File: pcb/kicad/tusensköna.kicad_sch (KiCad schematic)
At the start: 36 parts, among them J1 AudioJack3, J2 AudioJack3, J3 Micro_SD_Card, SW1 SW_Push, SW2 SW_Push, U1 Electrosmith_Daisy_Seed_Rev4

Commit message: issues fixed
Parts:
- removed 3V3A1, 3V3D1, A0, A6, GND1, MI1, MO1, SCK1, SCL1, SDA1, SS1, VIN1: Conn_01x01, Connector_Wire:SolderWire-0.5sqmm_1x01_D0.9mm_OD2.1mm, symbol Connector_Generic:Conn_01x01
- added J4: Conn_01x12_Pin, Connector_PinHeader_2.54mm:PinHeader_1x12_P2.54mm_Vertical, symbol Connector:Conn_01x12_Pin
- added JP1, JP2: Jumper_2_Bridged, Connector_PinHeader_2.54mm:PinHeader_1x02_P2.54mm_Vertical, symbol Jumper:Jumper_2_Bridged
- added R10, R9: 4.7k, Resistor_SMD:R_0805_2012Metric, symbol Device:R
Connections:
- net 3V3A: now also J4.12 (Pin_12)
- net 3V3D: now also J4.9 (Pin_9)
- net ADC0: now also J4.11 (Pin_11)
- net ADC6: now also J4.10 (Pin_10)
- net AGND: now also J4.8 (Pin_8)
- net SCL: now also J4.5 (Pin_5), JP1.2 (B), R9.2; no longer U1.13 (I2C1_SDA)
- net SDA: now also J4.6 (Pin_6), JP2.2 (B), R10.2; no longer U1.12 (I2C1_SCL)
- net SPI_CS: now also J4.1 (Pin_1)
- net SPI_PICO: now also J4.4 (Pin_4)
- net SPI_POCI: now also J4.3 (Pin_3)
- net SPI_SCK: now also J4.2 (Pin_2)
- net VIN: now also J4.7 (Pin_7)
- new net: JP1.1 (A), R9.1, U1.12 (I2C1_SCL)
- new net: JP2.1 (A), R10.1, U1.13 (I2C1_SDA)

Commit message: pullup
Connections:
- net 3V3D: now also JP1.1 (A), JP2.1 (A)
- net SCL: now also U1.12 (I2C1_SCL); no longer JP1.2 (B)
- net SDA: now also U1.13 (I2C1_SDA); no longer JP2.2 (B)
- new net: JP1.2 (B), R9.1
- new net: JP2.2 (B), R10.1
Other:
- moved on the sheet: JP1, JP2, R10, R9

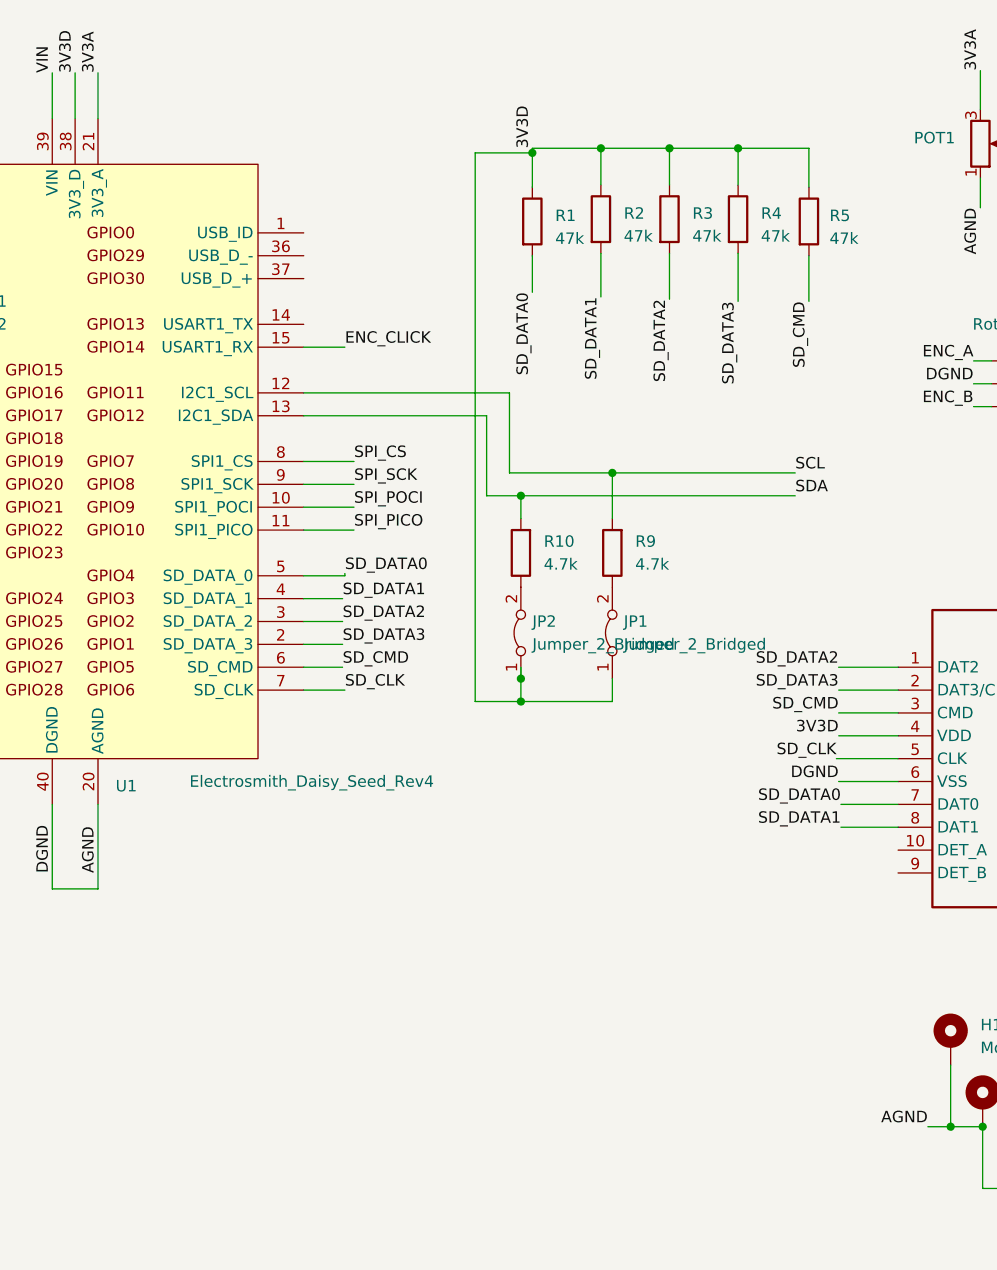
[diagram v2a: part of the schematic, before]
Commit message: schematic and gnd plane
Fixed errors where connection to gnd plane was insufficient for some components.
Moved some components to make space for heat dissipation.
Cleaned up part of schematic regarding pullup resistors.
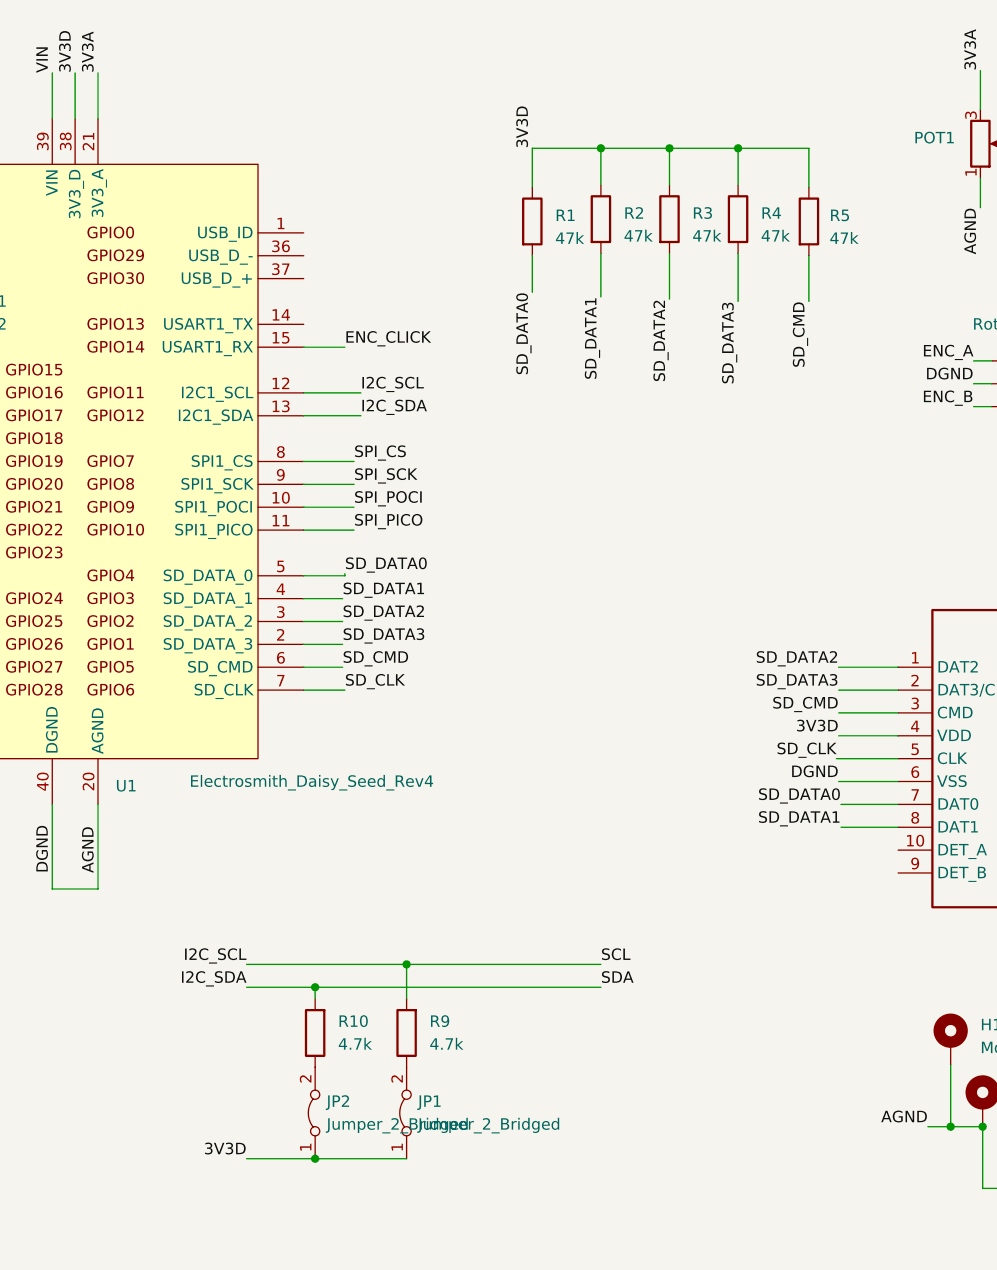
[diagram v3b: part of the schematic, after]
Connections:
- net SCL renamed I2C_SCL
- net SDA renamed I2C_SDA
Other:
- moved on the sheet: JP1, JP2, R10, R9
